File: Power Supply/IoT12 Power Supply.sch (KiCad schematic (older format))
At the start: 11 parts, among them J1 Screw_Terminal_01x03, J2 Screw_Terminal_01x03

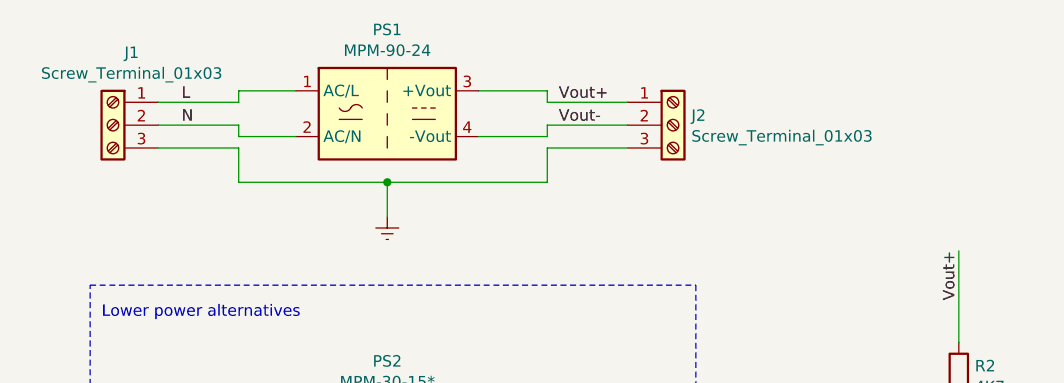
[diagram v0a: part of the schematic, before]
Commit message: Rotated J1, J2.
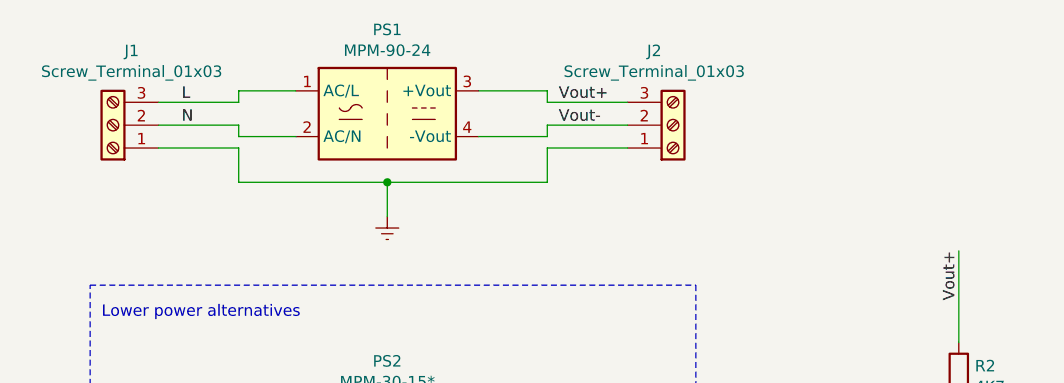
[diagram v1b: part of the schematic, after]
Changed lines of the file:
@@
 U 1 1 6038EB43
 P 4300 2450
-F 0 "J1" H 4218 2767 50  0000 C CNN
-F 1 "Screw_Terminal_01x03" H 4218 2676 50  0000 C CNN
+F 0 "J1" H 4218 2125 50  0000 C CNN
+F 1 "Screw_Terminal_01x03" H 4218 2216 50  0000 C CNN
 F 2 "TerminalBlock:TerminalBlock_bornier-3_P5.08mm" H 4300 2450 50  0001 C CNN
 F 3 "~" H 4300 2450 50  0001 C CNN
 	1    4300 2450
-	-1   0    0    -1
+	-1   0    0    1
 $EndComp
 $Comp
@@
 U 1 1 60390401
 P 6750 2450
-F 0 "J2" H 6830 2492 50  0000 L CNN
-F 1 "Screw_Terminal_01x03" H 6830 2401 50  0000 L CNN
+F 0 "J2" H 6668 2125 50  0000 C CNN
+F 1 "Screw_Terminal_01x03" H 6668 2216 50  0000 C CNN
 F 2 "TerminalBlock:TerminalBlock_bornier-3_P5.08mm" H 6750 2450 50  0001 C CNN
 F 3 "~" H 6750 2450 50  0001 C CNN
 	1    6750 2450
-	1    0    0    -1
+	1    0    0    1
 $EndComp
 Wire Wire Line
